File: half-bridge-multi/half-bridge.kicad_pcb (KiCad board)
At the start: 2 copper layers, 98.6 x 98.6 mm, 42 parts, among them J1 NegBus, J12 Bridge1, J2 PosBus, J27 Conn_01x01, J28 Conn_01x01, J3 Conn_01x01, J4 Conn_01x01, J5 Conn_01x01, J6 Conn_01x01, J7 Screw_Terminal_01x02, J8 Screw_Terminal_01x02, J9 Bridge1, Q1 Q_NIGBT_GCE, Q2 Q_NIGBT_GCE, Q3 Q_NIGBT_GCE, Q4 Q_NIGBT_GCE, Q5 Q_NIGBT_GCE, Q6 Q_NIGBT_GCE, Q7 Q_NIGBT_GCE, Q8 Q_NIGBT_GCE

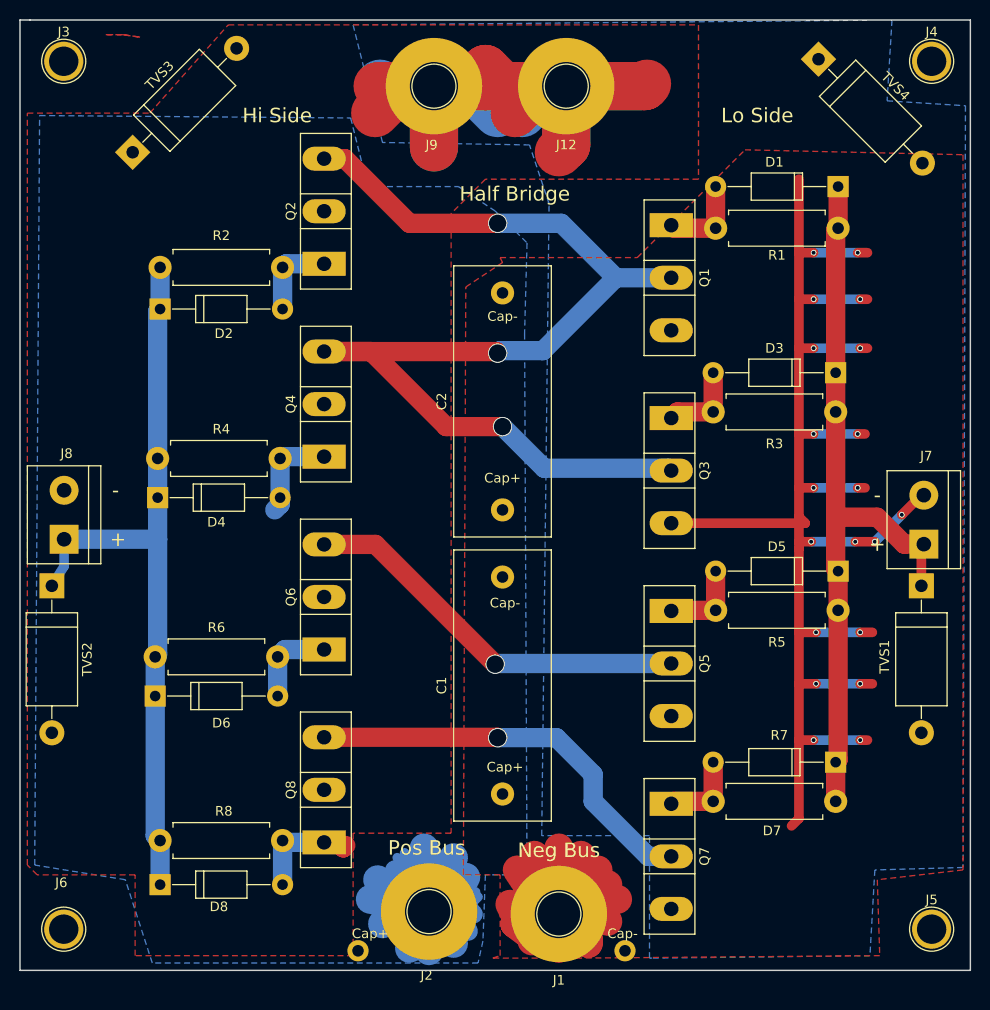
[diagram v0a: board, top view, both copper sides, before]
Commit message: Cleaned up labels and pads on half/full bridge boards
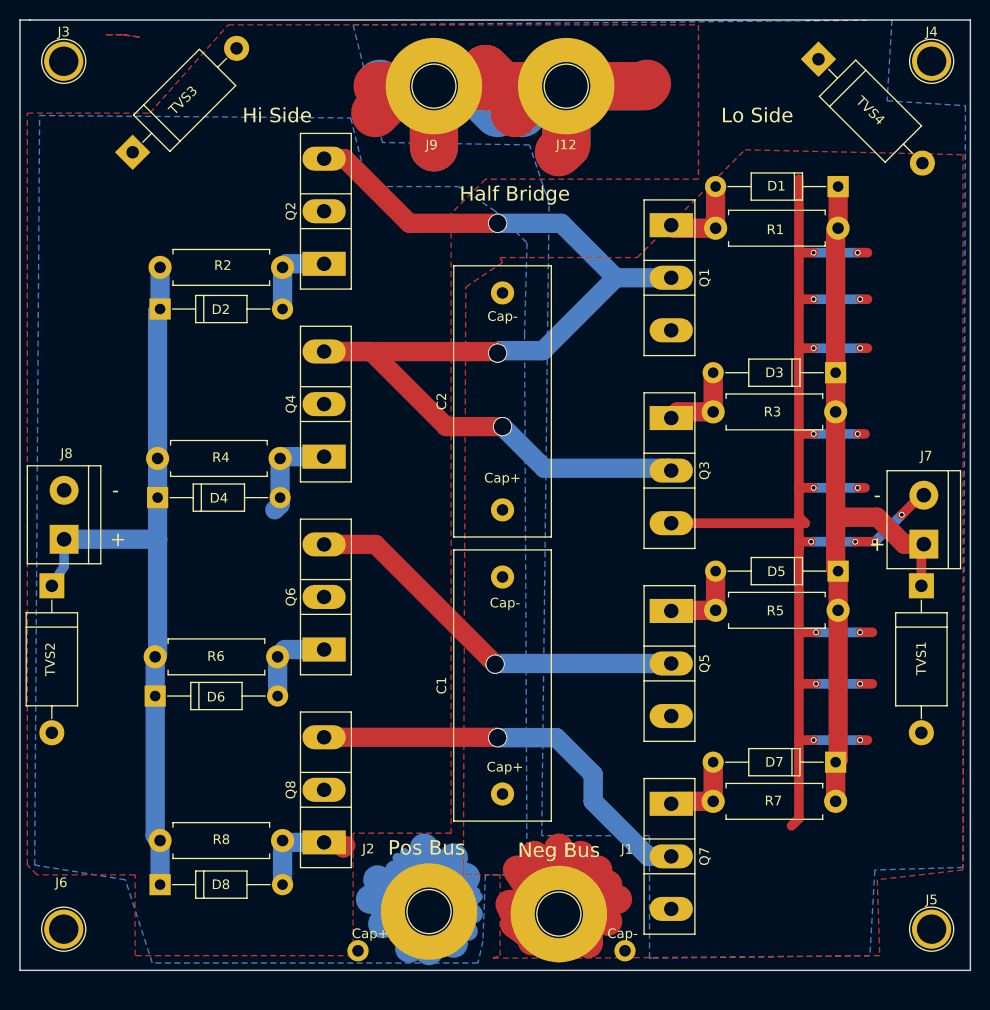
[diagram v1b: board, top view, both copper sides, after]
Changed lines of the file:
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@@
     (links 65)
     (no_connects 0)
-    (area 44.128 45.24564 145.347 146.363)
+    (area 45.390999 45.644999 144.093001 144.347001)
     (thickness 1.6)
     (drawings 20)
@@
   )
   (setup
-    (last_trace_width 2)
+    (last_trace_width 0.25)
     (user_trace_width 0.5)
     (user_trace_width 1)
@@
     (descr "module 1 pin (ou trou mecanique de percage)")
     (tags DEV)
-    (fp_text reference J2 (at -0.254 6.604) (layer F.SilkS)
+    (fp_text reference J2 (at -6.2992 -6.5024) (layer F.SilkS)
       (effects (font (size 1 1) (thickness 0.15)))
     )
@@
     (descr "Resistor, Axial_DIN0411 series, Axial, Horizontal, pin pitch=12.7mm, 1W = 1/1W, length*diameter=9.9*3.6mm^2")
     (tags "Resistor Axial_DIN0411 series Axial Horizontal pin pitch 12.7mm 1W = 1/1W length 9.9mm diameter 3.6mm")
-    (fp_text reference R6 (at 6.35 3.048 180) (layer F.SilkS)
+    (fp_text reference R6 (at 6.398 0.0508 180) (layer F.SilkS)
       (effects (font (size 1 1) (thickness 0.15)))
     )
@@
     (descr "Resistor, Axial_DIN0411 series, Axial, Horizontal, pin pitch=12.7mm, 1W = 1/1W, length*diameter=9.9*3.6mm^2")
     (tags "Resistor Axial_DIN0411 series Axial Horizontal pin pitch 12.7mm 1W = 1/1W length 9.9mm diameter 3.6mm")
-    (fp_text reference R8 (at 6.096 3.048 180) (layer F.SilkS)
+    (fp_text reference R8 (at 6.3472 0.1016 180) (layer F.SilkS)
       (effects (font (size 1 1) (thickness 0.15)))
     )
@@
     (descr "Resistor, Axial_DIN0411 series, Axial, Horizontal, pin pitch=12.7mm, 1W = 1/1W, length*diameter=9.9*3.6mm^2")
     (tags "Resistor Axial_DIN0411 series Axial Horizontal pin pitch 12.7mm 1W = 1/1W length 9.9mm diameter 3.6mm")
-    (fp_text reference R1 (at 6.35 2.794) (layer F.SilkS)
+    (fp_text reference R1 (at 6.1976 0.1524) (layer F.SilkS)
       (effects (font (size 1 1) (thickness 0.15)))
     )
@@
     (descr "D, DO-41_SOD81 series, Axial, Horizontal, pin pitch=12.7mm, , length*diameter=5.2*2.7mm^2, , http://www.diodes.com/_files/packages/DO-41%20(Plastic).pdf")
     (tags "D DO-41_SOD81 series Axial Horizontal pin pitch 12.7mm  length 5.2mm diameter 2.7mm")
-    (fp_text reference D5 (at 6.35 2.54 180) (layer F.SilkS)
+    (fp_text reference D5 (at 6.4008 -0.0508 180) (layer F.SilkS)
       (effects (font (size 1 1) (thickness 0.15)))
     )
@@
     (descr "Resistor, Axial_DIN0411 series, Axial, Horizontal, pin pitch=12.7mm, 1W = 1/1W, length*diameter=9.9*3.6mm^2")
     (tags "Resistor Axial_DIN0411 series Axial Horizontal pin pitch 12.7mm 1W = 1/1W length 9.9mm diameter 3.6mm")
-    (fp_text reference R4 (at 6.096 3.048 180) (layer F.SilkS)
+    (fp_text reference R4 (at 6.144 0.1016 180) (layer F.SilkS)
       (effects (font (size 1 1) (thickness 0.15)))
     )
@@
     (descr "D, DO-41_SOD81 series, Axial, Horizontal, pin pitch=12.7mm, , length*diameter=5.2*2.7mm^2, , http://www.diodes.com/_files/packages/DO-41%20(Plastic).pdf")
     (tags "D DO-41_SOD81 series Axial Horizontal pin pitch 12.7mm  length 5.2mm diameter 2.7mm")
-    (fp_text reference D2 (at 6.604 2.54) (layer F.SilkS)
+    (fp_text reference D2 (at 6.302 0.0508) (layer F.SilkS)
       (effects (font (size 1 1) (thickness 0.15)))
     )
@@
     (descr "module 1 pin (ou trou mecanique de percage)")
     (tags DEV)
-    (fp_text reference J1 (at 0 -6.858 180) (layer F.SilkS)
+    (fp_text reference J1 (at -7.0612 6.7056 180) (layer F.SilkS)
       (effects (font (size 1 1) (thickness 0.15)))
     )
@@
     (descr "D, DO-41_SOD81 series, Axial, Horizontal, pin pitch=12.7mm, , length*diameter=5.2*2.7mm^2, , http://www.diodes.com/_files/packages/DO-41%20(Plastic).pdf")
     (tags "D DO-41_SOD81 series Axial Horizontal pin pitch 12.7mm  length 5.2mm diameter 2.7mm")
-    (fp_text reference D1 (at 6.604 2.54 180) (layer F.SilkS)
+    (fp_text reference D1 (at 6.4008 0.0508 180) (layer F.SilkS)
       (effects (font (size 1 1) (thickness 0.15)))
     )
@@
     (descr "D, DO-41_SOD81 series, Axial, Horizontal, pin pitch=12.7mm, , length*diameter=5.2*2.7mm^2, , http://www.diodes.com/_files/packages/DO-41%20(Plastic).pdf")
     (tags "D DO-41_SOD81 series Axial Horizontal pin pitch 12.7mm  length 5.2mm diameter 2.7mm")
-    (fp_text reference D3 (at 6.35 2.54 180) (layer F.SilkS)
+    (fp_text reference D3 (at 6.35 0 180) (layer F.SilkS)
       (effects (font (size 1 1) (thickness 0.15)))
     )
@@
     (descr "D, DO-41_SOD81 series, Axial, Horizontal, pin pitch=12.7mm, , length*diameter=5.2*2.7mm^2, , http://www.diodes.com/_files/packages/DO-41%20(Plastic).pdf")
     (tags "D DO-41_SOD81 series Axial Horizontal pin pitch 12.7mm  length 5.2mm diameter 2.7mm")
-    (fp_text reference D4 (at 6.096 2.54) (layer F.SilkS)
+    (fp_text reference D4 (at 6.3528 0.0508) (layer F.SilkS)
       (effects (font (size 1 1) (thickness 0.15)))
     )
@@
     (descr "D, DO-41_SOD81 series, Axial, Horizontal, pin pitch=12.7mm, , length*diameter=5.2*2.7mm^2, , http://www.diodes.com/_files/packages/DO-41%20(Plastic).pdf")
     (tags "D DO-41_SOD81 series Axial Horizontal pin pitch 12.7mm  length 5.2mm diameter 2.7mm")
-    (fp_text reference D6 (at 6.858 2.794) (layer F.SilkS)
+    (fp_text reference D6 (at 6.302 0.1016) (layer F.SilkS)
       (effects (font (size 1 1) (thickness 0.15)))
     )
@@
     (descr "D, DO-41_SOD81 series, Axial, Horizontal, pin pitch=12.7mm, , length*diameter=5.2*2.7mm^2, , http://www.diodes.com/_files/packages/DO-41%20(Plastic).pdf")
     (tags "D DO-41_SOD81 series Axial Horizontal pin pitch 12.7mm  length 5.2mm diameter 2.7mm")
-    (fp_text reference D7 (at 6.604 -7.112 180) (layer F.SilkS)
+    (fp_text reference D7 (at 6.35 0 180) (layer F.SilkS)
       (effects (font (size 1 1) (thickness 0.15)))
     )
@@
     (descr "D, DO-41_SOD81 series, Axial, Horizontal, pin pitch=12.7mm, , length*diameter=5.2*2.7mm^2, , http://www.diodes.com/_files/packages/DO-41%20(Plastic).pdf")
     (tags "D DO-41_SOD81 series Axial Horizontal pin pitch 12.7mm  length 5.2mm diameter 2.7mm")
-    (fp_text reference D8 (at 6.096 2.286) (layer F.SilkS)
+    (fp_text reference D8 (at 6.302 0) (layer F.SilkS)
       (effects (font (size 1 1) (thickness 0.15)))
     )
@@
     (descr "Resistor, Axial_DIN0411 series, Axial, Horizontal, pin pitch=12.7mm, 1W = 1/1W, length*diameter=9.9*3.6mm^2")
     (tags "Resistor Axial_DIN0411 series Axial Horizontal pin pitch 12.7mm 1W = 1/1W length 9.9mm diameter 3.6mm")
-    (fp_text reference R2 (at 6.35 3.302 180) (layer F.SilkS)
+    (fp_text reference R2 (at 6.1948 0.2032 180) (layer F.SilkS)
       (effects (font (size 1 1) (thickness 0.15)))
     )
@@
     (descr "Resistor, Axial_DIN0411 series, Axial, Horizontal, pin pitch=12.7mm, 1W = 1/1W, length*diameter=9.9*3.6mm^2")
     (tags "Resistor Axial_DIN0411 series Axial Horizontal pin pitch 12.7mm 1W = 1/1W length 9.9mm diameter 3.6mm")
-    (fp_text reference R3 (at 6.35 3.302) (layer F.SilkS)
+    (fp_text reference R3 (at 6.1468 0) (layer F.SilkS)
       (effects (font (size 1 1) (thickness 0.15)))
     )
@@
     (descr "Resistor, Axial_DIN0411 series, Axial, Horizontal, pin pitch=12.7mm, 1W = 1/1W, length*diameter=9.9*3.6mm^2")
     (tags "Resistor Axial_DIN0411 series Axial Horizontal pin pitch 12.7mm 1W = 1/1W length 9.9mm diameter 3.6mm")
-    (fp_text reference R5 (at 6.35 3.302) (layer F.SilkS)
+    (fp_text reference R5 (at 6.1976 0.0508) (layer F.SilkS)
       (effects (font (size 1 1) (thickness 0.15)))
     )
@@
     (descr "Resistor, Axial_DIN0411 series, Axial, Horizontal, pin pitch=12.7mm, 1W = 1/1W, length*diameter=9.9*3.6mm^2")
     (tags "Resistor Axial_DIN0411 series Axial Horizontal pin pitch 12.7mm 1W = 1/1W length 9.9mm diameter 3.6mm")
-    (fp_text reference R7 (at 6.858 -6.858) (layer F.SilkS)
+    (fp_text reference R7 (at 6.2484 -0.0508) (layer F.SilkS)
       (effects (font (size 1 1) (thickness 0.15)))
     )
@@
     (descr "D, DO-201 series, Axial, Horizontal, pin pitch=15.24mm, , length*diameter=9.53*5.21mm^2, , http://www.diodes.com/_files/packages/DO-201.pdf")
     (tags "D DO-201 series Axial Horizontal pin pitch 15.24mm  length 9.53mm diameter 5.21mm")
-    (fp_text reference TVS3 (at 7.62 -3.665 45) (layer F.SilkS)
+    (fp_text reference TVS3 (at 7.507494 -0.107763 45) (layer F.SilkS)
       (effects (font (size 1 1) (thickness 0.15)))
     )
@@
     (descr "D, DO-201 series, Axial, Horizontal, pin pitch=15.24mm, , length*diameter=9.53*5.21mm^2, , http://www.diodes.com/_files/packages/DO-201.pdf")
     (tags "D DO-201 series Axial Horizontal pin pitch 15.24mm  length 9.53mm diameter 5.21mm")
-    (fp_text reference TVS4 (at 7.62 -3.665 315) (layer F.SilkS)
+    (fp_text reference TVS4 (at 7.579336 -0.035921 315) (layer F.SilkS)
       (effects (font (size 1 1) (thickness 0.15)))
     )
@@
     (descr "D, DO-201 series, Axial, Horizontal, pin pitch=15.24mm, , length*diameter=9.53*5.21mm^2, , http://www.diodes.com/_files/packages/DO-201.pdf")
     (tags "D DO-201 series Axial Horizontal pin pitch 15.24mm  length 9.53mm diameter 5.21mm")
-    (fp_text reference TVS1 (at 7.366 3.81 270) (layer F.SilkS)
+    (fp_text reference TVS1 (at 7.5184 0 270) (layer F.SilkS)
       (effects (font (size 1 1) (thickness 0.15)))
     )
@@
     (descr "D, DO-201 series, Axial, Horizontal, pin pitch=15.24mm, , length*diameter=9.53*5.21mm^2, , http://www.diodes.com/_files/packages/DO-201.pdf")
     (tags "D DO-201 series Axial Horizontal pin pitch 15.24mm  length 9.53mm diameter 5.21mm")
-    (fp_text reference TVS2 (at 7.62 -3.665 270) (layer F.SilkS)
-      (effects (font (size 1 1) (thickness 0.15)))
-    )
+    (fp_text reference TVS2 (at 7.62 0.1524 270) (layer F.SilkS)
+      (effects (font (size 1 1) (thickness 0.15)))
+    )
